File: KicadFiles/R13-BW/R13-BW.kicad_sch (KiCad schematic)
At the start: 30 parts, among them J1 Conn_01x01_Pin, J2 Conn_01x04_MountingPin, J3 Conn_01x04_MountingPin, SW1 SW_DPST_x2, SW2 SW_DPST_x2, U1 TPD4E05U06DQAR, U2 STM32F072CBTx, U3 XC6206PxxxMR

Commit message: Add and update KiCad design assets for R12/R13 variants
- refresh existing R12-AW, R13-AH, and R13-BW project files
- add the R13-AW project and variant-specific placer configs
- add 12u/13u outlines and normalize layout JSON filenames
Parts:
- removed H1: MountingHole_Pad, My-Fi Footprints:Cherry-GND-PAD, symbol Mechanical:MountingHole_Pad
- added D1, D10, D11, D12, D15, D16, D17, D18, D19, D2, D20, D21, D22, D23, D24, D25, D26, D29, D3, D32, D33, D34, D35, D36, D37, D38, D39, D4, D40, D41, D43, D45, D46, D47, D48, D49, D5, D51, D52, D54, D55, D56, D57, D58, D6, D7, D8, D9: 1N4148WS, My-Fi Footprints:D_SOD-323_HandSoldering, symbol Device:D
- added LED5: LED, My-Fi Footprints:CAPS_LED_MX_3mm, symbol Device:LED
- added MX1, MX12: MX_SW_solder, My-Fi Footprints:SW_MX_1.5u, symbol PCM_marbastlib-mx:MX_SW_solder
- added MX10, MX11, MX13, MX16, MX17, MX18, MX19, MX2, MX20, MX21, MX22, MX23, MX24, MX25, MX26, MX28, MX3, MX30, MX32, MX33, MX34, MX35, MX36, MX37, MX38, MX39, MX4, MX40, MX41, MX43, MX45, MX47, MX5, MX50, MX52, MX54, MX57, MX6, MX7, MX8, MX9: MX_SW_solder, My-Fi Footprints:SW_MX_1u, symbol PCM_marbastlib-mx:MX_SW_solder
- added MX14: MX_SW_solder, My-Fi Footprints:SW_MX_1.75u_STP_1.25, symbol PCM_marbastlib-mx:MX_SW_solder
- added MX15, MX42, MX44, MX51, MX53: MX_SW_solder, My-Fi Footprints:SW_MX_1.75u, symbol PCM_marbastlib-mx:MX_SW_solder
- added MX27, MX29, MX31, MX46, MX48, MX49, MX55, MX56, MX58: MX_SW_solder, My-Fi Footprints:SW_MX_1.25u, symbol PCM_marbastlib-mx:MX_SW_solder
- added R7: 220, Resistor_SMD:R_0402_1005Metric, symbol Device:R_Small
- added S13: MX_stab, My-Fi Footprints:STAB_MX_ISO-ROT, symbol PCM_marbastlib-mx:MX_stab
- added S26, S30: MX_stab, My-Fi Footprints:STAB_MX_2.25u, symbol PCM_marbastlib-mx:MX_stab
- added S43: MX_stab, My-Fi Footprints:STAB_MX_2.75u, symbol PCM_marbastlib-mx:MX_stab
- added S52: MX_stab, My-Fi Footprints:STAB_MX_6u_3u+3u, symbol PCM_marbastlib-mx:MX_stab
- C1, C2, C3, C4, C5, C6, C7, C8, C9: footprint Capacitor_SMD:C_0805_2012Metric_Pad1.18x1.45mm_HandSolder -> Capacitor_SMD:C_0402_1005Metric
- LED2: footprint My-Fi Footprints:CAPS_LED_MX_3mm -> My-Fi Footprints:DIP_LED_MX_3mm
- R1, R2, R3, R4, R5, R6: footprint Resistor_SMD:R_0805_2012Metric_Pad1.20x1.40mm_HandSolder -> Resistor_SMD:R_0402_1005Metric
- renumbered D1 to D201
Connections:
- net +5V: no longer J2.1 (Pin_1)
- net GND: now also LED5.1 (K)
- net VBUS: now also J2.1 (Pin_1)
- net LED_CAPS: now reaches U2.15 (PA5)
- net LED_CAPS: now also R7.2
- new net: D21.2 (A), MX21.2
- new net: D43.2 (A), MX42.2, MX43.2, MX44.2
- new net: D26.2 (A), MX26.2, MX27.2
- new net: D19.2 (A), MX19.2
- new net: D23.2 (A), MX23.2
- new net: D6.2 (A), MX6.2
- new net: D15.2 (A), MX14.2, MX15.2
- new net: D32.2 (A), MX30.2, MX31.2, MX32.2
- new net: D54.2 (A), MX53.2, MX54.2
- new net: D5.2 (A), MX5.2
- new net: LED5.2 (A), R7.1
- new net: D37.2 (A), MX37.2
- new net: D18.2 (A), MX18.2
- new net: D52.2 (A), MX52.2
- new net: D17.2 (A), MX17.2
- new net: D8.2 (A), MX8.2
- new net: D11.2 (A), MX11.2
- new net: D49.2 (A), MX49.2
- new net: D39.2 (A), MX39.2
- new net: D20.2 (A), MX20.2
- new net: D36.2 (A), MX36.2
- new net: D16.2 (A), MX16.2
- new net: D22.2 (A), MX22.2
- new net: D29.2 (A), MX28.2, MX29.2
- new net: D40.2 (A), MX40.2
- new net: D4.2 (A), MX4.2
- new net: D12.2 (A), MX12.2, MX13.2
- new net: D47.2 (A), MX47.2
- new net: D41.2 (A), MX41.2
- new net: D10.2 (A), MX10.2
- new net: D56.2 (A), MX56.2
- new net: D3.2 (A), MX3.2
- new net: D34.2 (A), MX34.2
- new net: D51.2 (A), MX50.2, MX51.2
- new net: D2.2 (A), MX2.2
- new net: D55.2 (A), MX55.2
- new net: D58.2 (A), MX58.2
- new net: D48.2 (A), MX48.2
- new net: D25.2 (A), MX25.2
- new net: D7.2 (A), MX7.2
- new net: D24.2 (A), MX24.2
- new net: D57.2 (A), MX57.2
- new net: D9.2 (A), MX9.2
- new net: D33.2 (A), MX33.2
- new net: D46.2 (A), MX46.2
- new net: D35.2 (A), MX35.2
- new net: D38.2 (A), MX38.2
- new net: D1.2 (A), MX1.2
- new net: D45.2 (A), MX45.2
- new net Col0: MX1.1, MX14.1, MX15.1, MX28.1, MX29.1, MX46.1
- new net Col1: MX16.1, MX2.1, MX30.1, MX31.1, MX32.1, MX47.1
- new net Col10: MX11.1, MX25.1, MX41.1, MX57.1
- new net Col11: MX12.1, MX13.1, MX26.1, MX27.1, MX42.1, MX43.1, MX44.1
- new net Col12: MX45.1, MX58.1
- new net Col2: MX17.1, MX3.1, MX33.1, MX48.1
- new net Col3: MX18.1, MX34.1, MX4.1, MX49.1
- new net Col4: MX19.1, MX35.1, MX5.1, MX50.1, MX51.1
- new net Col5: MX20.1, MX36.1, MX52.1, MX6.1
- new net Col6: MX21.1, MX37.1, MX7.1
- new net Col7: MX22.1, MX38.1, MX53.1, MX54.1, MX8.1
- new net Col8: MX23.1, MX39.1, MX55.1, MX9.1
- new net Col9: MX10.1, MX24.1, MX40.1, MX56.1
- new net Row0: D1.1 (K), D10.1 (K), D11.1 (K), D12.1 (K), D2.1 (K), D3.1 (K), D4.1 (K), D5.1 (K), D6.1 (K), D7.1 (K), D8.1 (K), D9.1 (K)
- new net Row1: D15.1 (K), D16.1 (K), D17.1 (K), D18.1 (K), D19.1 (K), D20.1 (K), D21.1 (K), D22.1 (K), D23.1 (K), D24.1 (K), D25.1 (K), D26.1 (K)
- new net Row2: D29.1 (K), D32.1 (K), D33.1 (K), D34.1 (K), D35.1 (K), D36.1 (K), D37.1 (K), D38.1 (K), D39.1 (K), D40.1 (K), D41.1 (K), D43.1 (K), D45.1 (K)
- new net Row3: D46.1 (K), D47.1 (K), D48.1 (K), D49.1 (K), D51.1 (K), D52.1 (K), D54.1 (K), D55.1 (K), D56.1 (K), D57.1 (K), D58.1 (K)
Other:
- note added: "LED CAPS"

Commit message: Add junctions and wires to R13-BW schematic for improved connectivity
- Added a junction at (300.99, 62.23) to enhance signal routing.
- Introduced a junction at (306.07, 67.31) for better circuit integration.
- Removed unnecessary junction at (299.72, 44.45) to clean up the schematic.
- Updated wire connections to reflect new junction placements and maintain circuit integrity.
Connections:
- net at D26.2 (A), MX26.2, MX27.2: now also MX13.2
- net at D12.2 (A), MX12.2: no longer MX13.2
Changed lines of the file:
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@@
+	)
+	(junction
+		(at 300.99 62.23)
+		(diameter 0)
+		(color 0 0 0 0)
 	)
 	(junction
@@
 	)
 	(junction
+		(at 306.07 67.31)
+		(diameter 0)
+		(color 0 0 0 0)
+	)
+	(junction
 		(at 161.29 224.79)
 		(diameter 0)
@@
 	)
 	(junction
-		(at 299.72 44.45)
-		(diameter 0)
-		(color 0 0 0 0)
-	)
-	(junction
 		(at 186.69 214.63)
 		(diameter 0)
@@
 	(wire
 		(pts
-			(xy 299.72 44.45) (xy 306.07 44.45)
-		)
-		(stroke
-			(width 0)
-			(type default)
-		)
-	)
-	(wire
-		(pts
 			(xy 294.64 62.23) (xy 294.64 85.09)
 		)
@@
 	(wire
 		(pts
+			(xy 300.99 39.37) (xy 300.99 62.23)
+		)
+		(stroke
+			(width 0)
+			(type default)
+		)
+	)
+	(wire
+		(pts
 			(xy 71.12 120.65) (xy 93.98 120.65)
 		)
@@
 	(wire
 		(pts
-			(xy 294.64 39.37) (xy 300.99 39.37)
-		)
-		(stroke
-			(width 0)
-			(type default)
-		)
-	)
-	(wire
-		(pts
 			(xy 88.9 39.37) (xy 88.9 62.23)
 		)
@@
 		)
 		(stroke
+			(width 0)
+			(type default)
+		)
+	)
+	(wire
+		(pts
+			(xy 306.07 44.45) (xy 306.07 67.31)
+		)
+		(stroke

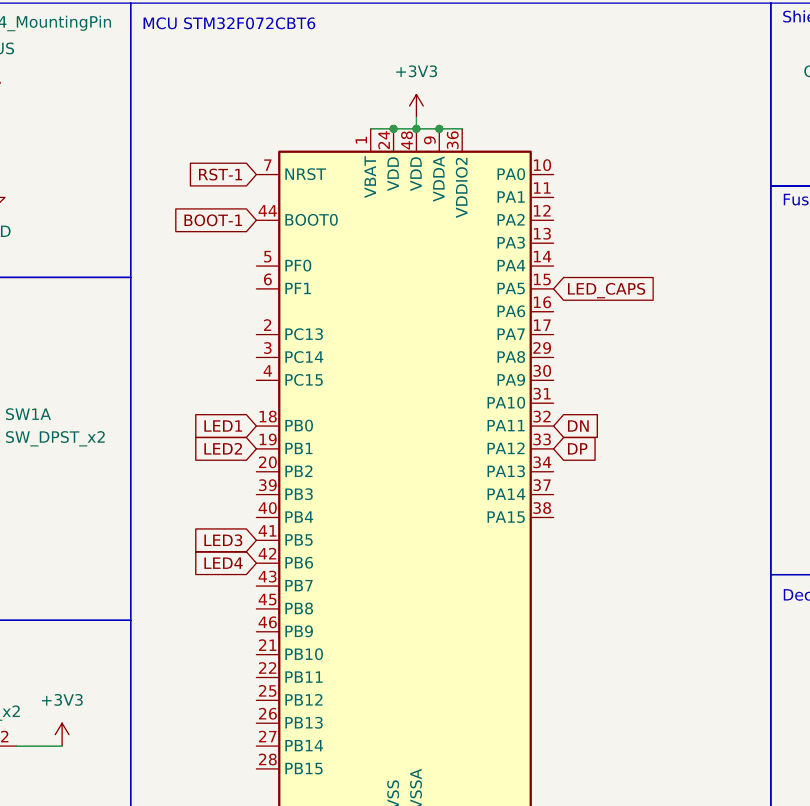
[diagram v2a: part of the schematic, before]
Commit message: Update design rules and add global labels in schematic
- Changed design rule for "courtyards_overlap" from "error" to "ignore".
- Updated hole clearance and hole to hole rules to "ignore".
- Set several silk layer rules to "ignore" to reduce warnings.
- Added multiple global labels in the schematic for better intersheet referencing, including "Col0", "Col1", "Col2", "Col3", "Col4", "Col5", "Col6", "Col7", "Col8", "Col9", "Col10", "Col11", "Col12", "Row0", "Row1", "Row2", and "Row3".
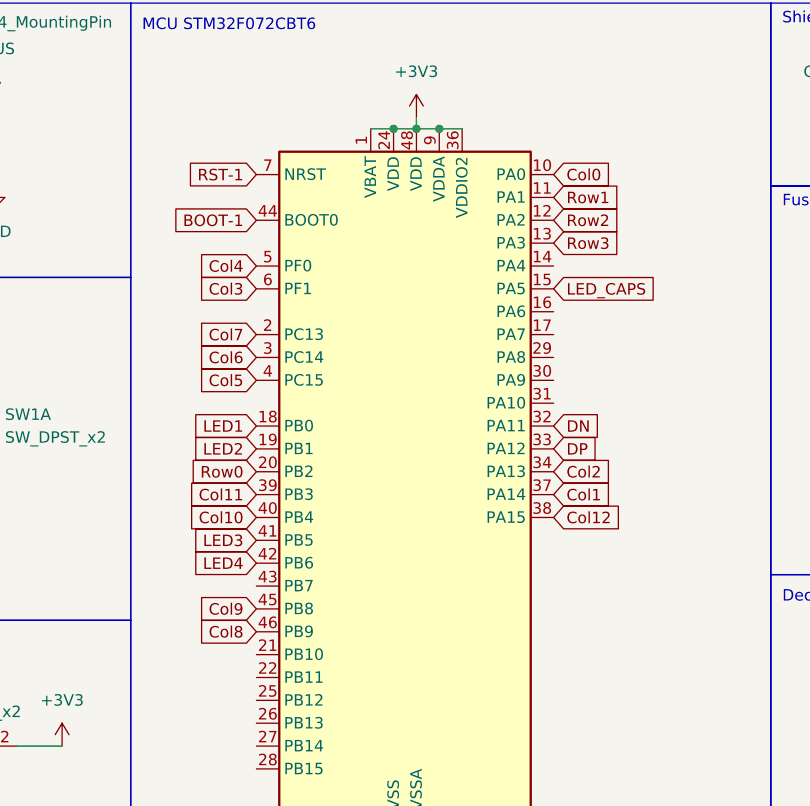
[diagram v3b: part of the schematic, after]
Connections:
- net Col0: now also U2.10 (PA0)
- net Col1: now also U2.37 (PA14)
- net Col10: now also U2.40 (PB4)
- net Col11: now also U2.39 (PB3)
- net Col12: now also U2.38 (PA15)
- net Col2: now also U2.34 (PA13)
- net Col3: now also U2.6 (PF1)
- net Col4: now also U2.5 (PF0)
- net Col5: now also U2.4 (PC15)
- net Col6: now also U2.3 (PC14)
- net Col7: now also U2.2 (PC13)
- net Col8: now also U2.46 (PB9)
- net Col9: now also U2.45 (PB8)
- net Row0: now also U2.20 (PB2)
- net Row1: now also U2.11 (PA1)
- net Row2: now also U2.12 (PA2)
- net Row3: now also U2.13 (PA3)
